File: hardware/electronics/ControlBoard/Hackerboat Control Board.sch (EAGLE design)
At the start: 178 parts, among them J3 3-1437664-0, U1 IPS6044, U14 TPS54331, U15 TPS54331, U2 ARDUINO-MEGAFULL, U3 IPS6044, U4 IPS6044, U5 IPS6044

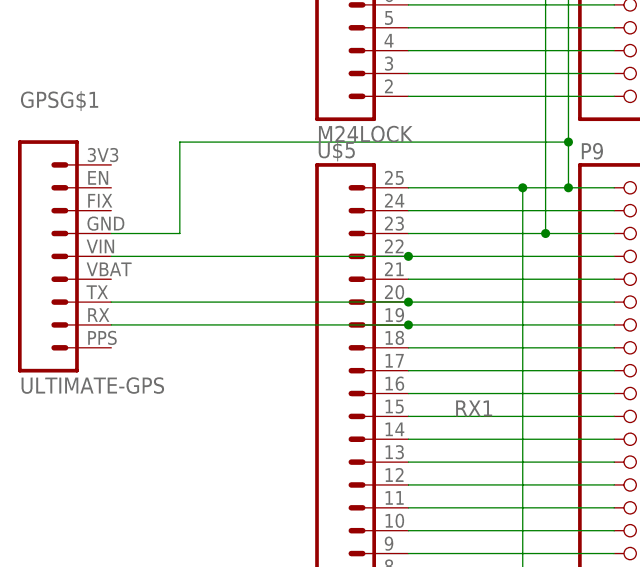
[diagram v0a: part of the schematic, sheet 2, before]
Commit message: Added hardware test code Various modifications to 'as-built' condition Added TODO.md
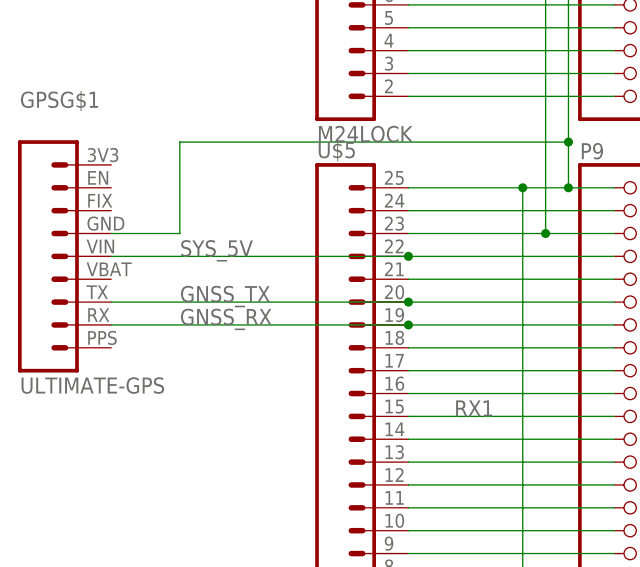
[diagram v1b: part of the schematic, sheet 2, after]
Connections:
- net N$1 renamed GNSS_RX
- net N$2 renamed GNSS_TX
- net N$67 renamed SYS_5V
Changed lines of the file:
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@@
 </segment>
 </net>
-<net name="N$1" class="0">
+<net name="GNSS_RX" class="0">
 <segment>
 <pinref part="GPS" gate="G$1" pin="2"/>
@@
 <wire x1="63.5" y1="106.68" x2="86.36" y2="106.68" width="0.1524" layer="91"/>
 <junction x="63.5" y="106.68"/>
-</segment>
-</net>
-<net name="N$2" class="0">
+<label x="38.1" y="106.68" size="1.778" layer="95"/>
+</segment>
+</net>
+<net name="GNSS_TX" class="0">
 <segment>
 <pinref part="GPS" gate="G$1" pin="3"/>
@@
 <wire x1="63.5" y1="109.22" x2="86.36" y2="109.22" width="0.1524" layer="91"/>
 <junction x="63.5" y="109.22"/>
+<label x="38.1" y="109.22" size="1.778" layer="95"/>
 </segment>
 </net>
@@
 </segment>
 </net>
-<net name="N$67" class="0">
+<net name="SYS_5V" class="0">
 <segment>
 <pinref part="GPS" gate="G$1" pin="5"/>
@@
 <wire x1="30.48" y1="114.3" x2="63.5" y2="114.3" width="0.1524" layer="91"/>
 <junction x="63.5" y="114.3"/>
-</segment>
-</net>
+<label x="38.1" y="114.3" size="1.778" layer="95"/>
+</segment>
+</net>

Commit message: Initial trimming of unnecessary parts in preparation for serious work. Keeping the power supply circuits, BBB connection, IMU, and GPS.
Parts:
- removed AUX, RELAY: 1751303, con-phoenix-350:1751303
- removed C1, C10, C11, C12, C2, C3, C4, C9: 1n, resistor:C-EUC0603
- removed C13, C14, C15, C16, C5, C6, C7, C8: 100n, resistor:C-EUC0603
- removed D1, D2: 3.3V, SparkFun-DiscreteSemi:DIODE-ZENER3.3V
- removed D10, D11, D12, D13, D14, D15, D16, D17, D18, D19, D20, D21, D22, D23, D24, D25, D26, D27, D28, D29, D3, D30, D31, D32, D33, D34, D4, D5, D6, D7, D8, D9: (no value), adafruit:DIODESOD-123
- removed F1, F4, F5, F6, F7, F8, F9: (no value), adafruit:PTCFUSE-1206
- removed H5, H6: MOUNT-PAD-ROUND5.5, holes:MOUNT-PAD-ROUND5.5
- removed HTU21D: HTU21D, sparkfun-sensor-boards:HTU21D
- removed I1/V2, I2/V3, I3/V4, I4: (no value), SparkFun-Connectors:M04LOCK_LONGPADS
- removed JP10, JP11, JP12, JP13, JP14: (no value), SparkFun-Connectors:M08LOCK
- removed JP15, JP16: M16LOCK, SparkFun-Connectors:M16LOCK
- removed JP17: (no value), SparkFun-Connectors:M06LOCK
- removed LED10, LED3, LED4, LED5, LED6, LED7, LED8, LED9: (no value), adafruit:LEDCHIPLED_0805
- removed R1, R2: 1K, resistor:R-EU_R0603
- removed R10, R17, R18, R9: 100K, res-cap-arrays:4R-NCTS742C083
- removed R11, R12, R13, R14, R15, R16, R3, R5, R6, R7, R8: 10K, res-cap-arrays:4R-NCTS742C083
- removed R25, R31, R32, R33, R34, R35, R36, R37: (no value), resistor:R-EU_R0603
- removed R29: 15K, resistor:R-EU_R0603
- removed R30: 10K, resistor:R-EU_R0603
- removed R4: 10k, res-cap-arrays:4R-NCTS742C083
- removed SERVO_AUX1, SERVO_AUX2, STEERING: (no value), SparkFun-Connectors:M03LOCK_LONGPADS
- removed U1, U3, U4, U5: IPS6044, logos-faves:IPS6044
- removed U10, U11, U12, U13, U6, U7, U8, U9: (no value), allegro3:ACS712
- removed U2: ARDUINO-MEGAFULL, SparkFun-Boards:ARDUINO-MEGAFULL
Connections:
- removed net +5V/1: C24.1, C25.1, L1.2, R22.2, R38.2, U$1.VDD_5V@1, U$1.VDD_5V@2, U$2.23, U$5.23
- removed net 13: JP14.3, U2.13
- removed net AUX1: JP15.9, R11A.1, U2.36
- removed net AUX1FB: JP16.9, R11B.1, U2.37
- removed net AUX1I: JP12.7, U2.A9, U6.VIO
- removed net AUX2: JP16.10, R12B.1, U2.35
- removed net AUX2FB: JP15.10, R11D.1, U2.34
- removed net AUX2I: JP12.8, U2.A8, U7.VIO
- removed net AUX3: JP15.11, R12C.1, U2.32
- removed net AUX3FB: JP16.11, R12D.1, U2.33
- removed net AUX3I: JP11.1, U2.A7, U8.VIO
- removed net AUX4: JP16.12, R13D.1, U2.31
- removed net AUX4FB: JP15.12, R13C.1, U2.30
- removed net AUX4I: JP11.2, U2.A6, U9.VIO
- removed net AUX5: JP15.13, R14A.1, U2.28
- removed net AUX5FB: JP16.13, R14B.1, U2.29
- removed net AUX5I: JP11.3, U10.VIO, U2.A5
- removed net AUX6: JP16.14, R15B.1, U2.27
- removed net AUX6FB: JP15.14, R14D.1, U2.26
- removed net AUX6I: JP11.4, U11.VIO, U2.A4
- removed net AUX7: JP15.15, R15C.1, U2.24
- removed net AUX7FB: JP16.15, R16A.1, U2.25
- removed net AUX7I: JP11.5, U12.VIO, U2.A3
- removed net AUX8: JP16.16, R16D.1, U2.23
- removed net AUX8FB: JP15.16, R16C.1, U2.22
- removed net AUX8I: JP11.6, U13.VIO, U2.A2
- removed net I1: I1/V2.2, JP12.6, U2.A10
- removed net I2: I2/V3.2, JP12.3, U2.A13
- removed net I3: I3/V4.2, JP12.4, U2.A12
- removed net I4: I4.2, JP12.5, U2.A11
- removed net N$10: D7.C, D8.A, LED5.A, R9B.1, RELAY-3.K, U1.OUT3@0, U1.OUT3@1, U1.OUT3@2
- removed net N$100: JP14.7, U2.9
- removed net N$101: JP14.6, U2.10
- removed net N$102: JP14.5, U2.11
- removed net N$103: JP14.4, U2.12
- removed net N$11: D10.A, D9.C, LED6.A, R9A.1, RELAY-4.K, U1.OUT4@0, U1.OUT4@1, U1.OUT4@2
- removed net N$12: R4A.2, U1.IN1
- removed net N$13: R5B.2, U1.IN2
- removed net N$14: R5C.2, U1.IN3
- removed net N$15: R3D.2, U1.IN4
- removed net N$16: R4B.2, R4C.2, U1.DG1
- removed net N$17: R4D.2, R5A.2, U1.DG2
- removed net N$178: LED3.C, R25.2
- removed net N$179: LED4.C, R31.2
- removed net N$18: R3A.2, R5D.2, U1.DG3
- removed net N$180: LED5.C, R32.2
- removed net N$181: LED6.C, R33.2
- removed net N$186: LED7.C, R34.2
- removed net N$187: LED8.C, R35.2
- removed net N$188: LED9.C, R36.2
- removed net N$189: LED10.C, R37.2
- removed net N$19: R3B.2, R3C.2, U1.DG4
- removed net N$20: R7B.2, U3.IN2
- removed net N$21: R6D.2, R7A.2, U3.DG2
- removed net N$22: R6B.2, R6C.2, U3.DG1
- removed net N$23: R7D.2, R8A.2, U3.DG3
- removed net N$24: R8B.2, R8C.2, U3.DG4
- removed net N$25: D11.C, D12.A, LED7.A, R10D.1, RELAY-5.K, U3.OUT1@0, U3.OUT1@1, U3.OUT1@2
- removed net N$26: D13.C, D14.A, LED8.A, R10C.1, RELAY-6.K, U3.OUT2@0, U3.OUT2@1, U3.OUT2@2
- removed net N$27: D15.C, D16.A, LED9.A, R10B.1, RELAY-7.K, U3.OUT3@0, U3.OUT3@1, U3.OUT3@2
- removed net N$28: D17.C, D18.A, LED10.A, R10A.1, RELAY-8.K, U3.OUT4@0, U3.OUT4@1, U3.OUT4@2
- removed net N$29: D25.C, D26.A, R17A.1, U4.OUT4@0, U4.OUT4@1, U4.OUT4@2, U9.IP+@0, U9.IP+@1
- removed net N$3: JP13.4, R1.1, U2.18(TX1)
- removed net N$30: AUX-2.K, U7.IP-@0, U7.IP-@1
- removed net N$31: AUX-3.K, U8.IP-@0, U8.IP-@1
- removed net N$32: AUX-4.K, U9.IP-@0, U9.IP-@1
- removed net N$33: AUX-5.K, U10.IP-@0, U10.IP-@1
- removed net N$34: D19.C, D20.A, R17D.1, U4.OUT1@0, U4.OUT1@1, U4.OUT1@2, U6.IP+@0, U6.IP+@1
- removed net N$35: D21.C, D22.A, R17C.1, U4.OUT2@0, U4.OUT2@1, U4.OUT2@2, U7.IP+@0, U7.IP+@1
- removed net N$36: D23.C, D24.A, R17B.1, U4.OUT3@0, U4.OUT3@1, U4.OUT3@2, U8.IP+@0, U8.IP+@1
- removed net N$37: AUX-1.K, U6.IP-@0, U6.IP-@1
- removed net N$38: R11A.2, U4.IN1
- removed net N$39: R12B.2, U4.IN2
- removed net N$4: JP10.7, R2.2, U2.1(TX0)
- removed net N$40: R12C.2, U4.IN3
- removed net N$41: R13D.2, U4.IN4
- removed net N$42: R11B.2, R11C.2, U4.DG1
- removed net N$43: R11D.2, R12A.2, U4.DG2
- removed net N$44: R12D.2, R13A.2, U4.DG3
- removed net N$45: R13B.2, R13C.2, U4.DG4
- removed net N$46: R14A.2, U5.IN1
- removed net N$47: R16D.2, U5.IN4
- removed net N$48: R15C.2, U5.IN3
- removed net N$49: R15B.2, U5.IN2
- removed net N$5: R6A.2, U3.IN1
- removed net N$50: R14B.2, R14C.2, U5.DG1
- removed net N$51: R14D.2, R15A.2, U5.DG2
- removed net N$52: R15D.2, R16A.2, U5.DG3
- removed net N$53: R16B.2, R16C.2, U5.DG4
- removed net N$54: D27.C, D28.A, R18D.1, U10.IP+@0, U10.IP+@1, U5.OUT1@0, U5.OUT1@1, U5.OUT1@2
- removed net N$55: D29.C, D30.A, R18C.1, U11.IP+@0, U11.IP+@1, U5.OUT2@0, U5.OUT2@1, U5.OUT2@2
- removed net N$56: D31.C, D32.A, R18B.1, U12.IP+@0, U12.IP+@1, U5.OUT3@0, U5.OUT3@1, U5.OUT3@2
- removed net N$57: D33.C, D34.A, R18A.1, U13.IP+@0, U13.IP+@1, U5.OUT4@0, U5.OUT4@1, U5.OUT4@2
- removed net N$58: AUX-6.K, U11.IP-@0, U11.IP-@1
- removed net N$59: AUX-7.K, U12.IP-@0, U12.IP-@1
- removed net N$6: R8D.2, U3.IN4
- removed net N$60: AUX-8.K, U13.IP-@0, U13.IP-@1
- removed net N$61: C1.2, U6.FILT
- removed net N$64: C2.2, U7.FILT
- removed net N$65: C3.2, U8.FILT
- removed net N$66: C4.2, U9.FILT
- removed net N$7: R7C.2, U3.IN3
- removed net N$74: C9.2, U10.FILT
- removed net N$75: C10.2, U11.FILT
- removed net N$76: C11.2, U12.FILT
- removed net N$77: C12.2, U13.FILT
- removed net N$8: D3.C, D4.A, LED3.A, R9D.1, RELAY-1.K, U1.OUT1@0, U1.OUT1@1, U1.OUT1@2
- removed net N$83: F1.2, I1/V2.1
- removed net N$86: F4.2, I2/V3.1
- removed net N$87: F5.2, I3/V4.1
- removed net N$88: F6.2, I4.1
- removed net N$89: F7.2, SERVO_AUX1.2
- removed net N$9: D5.C, D6.A, LED4.A, R9C.1, RELAY-2.K, U1.OUT2@0, U1.OUT2@1, U1.OUT2@2
- removed net N$90: F8.2, SERVO_AUX2.2
- removed net N$91: JP10.1, U2.7
- removed net N$92: JP10.2, U2.6
- removed net N$93: F9.2, STEERING.2
- removed net N$94: JP11.8, R29.1, R30.2, U2.A0
- removed net N$95: JP13.5, U2.17(RX2)
- removed net N$96: JP13.6, U2.16(TX2)
- removed net N$97: JP13.7, U2.15(RX3)
- removed net N$98: JP13.8, U2.14(TX3)
- removed net N$99: JP14.8, U2.8
- removed net RELAY1: JP15.1, R4A.1, U2.52
- removed net RELAY1FB: JP16.1, R4B.1, U2.53
- removed net RELAY2: JP16.2, R5B.1, U2.51
- removed net RELAY2FB: JP15.2, R5A.1, U2.50
- removed net RELAY3: JP15.3, R5C.1, U2.48
- removed net RELAY3FB: JP16.3, R5D.1, U2.49
- removed net RELAY4: JP16.4, R3D.1, U2.47
- removed net RELAY4FB: JP15.4, R3C.1, U2.46
- removed net RELAY5: JP15.5, R6A.1, U2.44
- removed net RELAY5FB: JP16.5, R6B.1, U2.45
- removed net RELAY6: JP16.6, R7B.1, U2.43
- removed net RELAY6FB: JP15.6, R6D.1, U2.42
- removed net RELAY7: JP15.7, R7C.1, U2.40
- removed net RELAY7FB: JP16.7, R7D.1, U2.41
- removed net RELAY8: JP16.8, R8D.1, U2.39
- removed net RELAY8FB: JP15.8, R8C.1, U2.38
- removed net SCL: HTU21D.4, IMUG$1.4, JP13.1, R19.1, U2.21(SCL)
- removed net SDA: HTU21D.3, IMUG$1.5, JP13.2, R20.1, U2.20(SDA)
- removed net SERVO_AUX1: JP10.4, SERVO_AUX1.3, U2.4
- removed net SERVO_AUX2: JP10.3, SERVO_AUX2.3, U2.5
- removed net STEERING: JP10.5, STEERING.3, U2.3
- removed net V2: I1/V2.3, JP11.7, U2.A1
- removed net V3: I2/V3.3, JP12.1, U2.A15
- removed net V4: I3/V4.3, JP12.2, U2.A14
- new net N$196: IMUG$1.5, R20.1
- new net N$197: IMUG$1.4, R19.1
- net +12V: no longer D10.C, D12.C, D14.C, D16.C, D18.C, D20.C, D22.C, D24.C, D26.C, D28.C, D30.C, D32.C, D34.C, D4.C, D6.C, D8.C, JP17.6, R10A.2, R10B.2, R10C.2, R10D.2, R17A.2, R17B.2, R17C.2, R17D.2, R18A.2, R18B.2, R18C.2, R18D.2, R29.2, R9A.2, R9B.2, R9C.2, R9D.2, U1.VCC@0, U1.VCC@1, U1.VCC@2, U1.VCC@3, U2.VIN, U3.VCC@0, U3.VCC@1, U3.VCC@2, U3.VCC@3, U4.VCC@0, U4.VCC@1, U4.VCC@2, U4.VCC@3, U5.VCC@0, U5.VCC@1, U5.VCC@2, U5.VCC@3
- net +3V3: no longer HTU21D.1, JP17.2, U2.3.3V
- net +5V: now also C24.1, C25.1, L1.2, R22.2, R38.2, U$1.VDD_5V@1, U$1.VDD_5V@2, U$2.23, U$5.23; no longer C13.2, C14.2, C15.2, C16.2, C5.2, C6.2, C7.2, C8.2, F1.1, F4.1, F5.1, F6.1, JP17.3, R11C.1, R12A.1, R13A.1, R13B.1, R14C.1, R15A.1, R15D.1, R16B.1, R3A.1, R3B.1, R4C.1, R4D.1, R6C.1, R7A.1, R8A.1, R8B.1, U10.VCC, U11.VCC, U12.VCC, U13.VCC, U2.5V@0, U2.5V@1, U2.5V@2, U6.VCC, U7.VCC, U8.VCC, U9.VCC
- net 7V4: no longer F7.1, F8.1, F9.1
- net GND: no longer C1.1, C10.1, C11.1, C12.1, C13.1, C14.1, C15.1, C16.1, C2.1, C3.1, C4.1, C5.1, C6.1, C7.1, C8.1, C9.1, D1.A, D11.A, D13.A, D15.A, D17.A, D19.A, D2.A, D21.A, D23.A, D25.A, D27.A, D29.A, D3.A, D31.A, D33.A, D5.A, D7.A, D9.A, H5.MOUNT, H6.MOUNT, HTU21D.2, I1/V2.4, I2/V3.4, I3/V4.4, I4.4, JP17.4, JP17.5, R25.1, R30.1, R31.1, R32.1, R33.1, R34.1, R35.1, R36.1, R37.1, SERVO_AUX1.1, SERVO_AUX2.1, STEERING.1, U1.GND@1, U1.GND@2, U1.GND@3, U1.GND@4, U10.GND, U11.GND, U12.GND, U13.GND, U2.GND@0, U2.GND@1, U2.GND@2, U2.GND@3, U2.GND@4, U3.GND@1, U3.GND@2, U3.GND@3, U3.GND@4, U4.GND@1, U4.GND@2, U4.GND@3, U4.GND@4, U5.GND@1, U5.GND@2, U5.GND@3, U5.GND@4, U6.GND, U7.GND, U8.GND, U9.GND
- net RX0: no longer JP10.8, U2.0(RX0)
- net RX1: no longer JP13.3, U2.19(RX1)
- net SERVO_EN: no longer JP10.6, U2.2
- net TX0: no longer D2.C, R2.1
- net TX1: no longer D1.C, R1.2

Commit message: First cut at the system block diagram
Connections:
- removed net N$118: U$1.VDD_3V3EXP@2, U$2.24
- removed net N$71: U$1.VDD_3V3EXP@1, U$5.24
- net +3V3: now also U$1.VDD_3V3EXP@1, U$1.VDD_3V3EXP@2, U$2.24, U$5.24
- net GND: no longer GPSG$1.6
- net GNSS_RX: no longer GPSG$1.2
- net GNSS_TX: no longer GPSG$1.3
- net SYS_5V: no longer GPSG$1.5
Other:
- note added: "Grounding"
- note added: "Main Systems Power"
- note added: "Servo Power"

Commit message: Everything in except the 15V boost converter and a couple of connectors
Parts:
- removed 5V/1-STAT: (no value), adafruit:LEDCHIPLED_0805
- added 5V-STAT: (no value), adafruit:LEDCHIPLED_0805
- added ACC_POWER: (no value), pinhead-1:PINHD-2X8_2.54
- added BBB_CONSOLE: FTDI_BASICPTH, SparkFun-Connectors:FTDI_BASICPTH
- added C1, C2, C3, C4, C5, C6: (no value), resistor:C-EUC0603
- added C10, C11, C12, C13, C14, C15, C16, C35, C36, C37, C38, C39, C7, C8, C9: 100n, resistor:C-EUC0603
- added D1, D10, D11, D12, D13, D14, D15, D16, D17, D18, D19, D2, D3, D4, D5, D6, D7, D8, D9: (no value), adafruit:DIODESOD-123
- added IC1: 74AHC1G08DBV, 74xx-little-us:74AHC1G08DBV
- added J1, J2: (no value), SparkFun-Connectors:M03LOCK
- added J4: (no value), SparkFun-Connectors:M05LOCK
- added J5: (no value), SparkFun-Connectors:M09LOCK
- added J6: (no value), SparkFun-Connectors:M10LOCK
- added J7: (no value), SparkFun-Connectors:M18_
- added MOTOR-CTRL-RELAYS: (no value), SparkFun-Connectors:DB9FEMALE
- added POE-DEVICE, POE-LAN: RJ45, SparkFun-Connectors:RJ45-8PTH
- added POWER_INPUT: 3-1437664-0, logos-headers:3-1437664-0
- added POWER_MONITOR: (no value), pinhead-1:PINHD-2X6_2.54
- added POWER_STATE: HEADER_POS5_70555, con-molex-c-grid-sl:HEADER_POS5_70555
- added R1, R13, R14, R15, R2, R25, R29, R3, R30, R34, R35, R36, R42, R43, R44, R48, R69, R7, R70, R71, R75, R76, R77, R8, R81, R82, R83, R9: 10K, resistor:R-EU_R0603
- added R10, R16, R31, R37, R4, R45, R72, R78, R84: 100K, resistor:R-EU_R0603
- added R11, R17, R32, R40, R46, R5, R55, R73, R79, R85: 0R05, resistor:R-EU_R2512
- added R12, R18, R33, R41, R47, R56, R6, R74, R80, R86: 33K, resistor:R-EU_R0603
- added R49, R50: (no value), resistor:R-EU_R0603
- added R51, R52, R53, R54: 4u7, resistor:R-EU_R0603
- added S1: FONA, adafruit-sensor-boards:FONA
- added SERIAL_CONSOLE: HEADER_POS4_70555, con-molex-c-grid-sl:HEADER_POS4_70555
- added STATUS_LIGHTS, STEERING: HEADER_POS3_70555, con-molex-c-grid-sl:HEADER_POS3_70555
- added U1, U11, U2, U20, U22, U24, U4, U6, U8: IPS6041G, hackerbot:IPS6041G
- added U10, U12, U21, U23, U25, U27, U3, U5, U7, U9: INA169, logos-power:INA169
- added U13, U16, U17: (no value), adafruit:TXB0108PWR
- added U18, U19: ADC128D818, ti-stuff:ADC128D818
- added U26: (no value), adafruit:TXS0102
- J3: value 3-1437664-0 -> (none); device logos-headers:3-1437664-0 -> SparkFun-Connectors:M04LOCK
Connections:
- net N$109 renamed BBB_MISO
- net N$168 renamed BBB_SCLK
- net N$169 renamed BBB_MOSI
- net RX1 renamed N$21
- net TX1 renamed BBB_STAT_LIGHT_3V3
- removed net 7V4: C26.1, C27.1, L2.2, R27.2, R39.2
- removed net N$105: U$1.AIN1, U$2.6
- removed net N$111: U$1.I2C2_SDA, U$2.16
- removed net N$112: U$1.I2C1_SDA, U$2.17
- removed net N$113: U$1.EHRPWM1B, U$2.18
- removed net N$114: U$1.EHRPWM1A, U$2.19
- removed net N$115: U$1.GPIO1_28, U$2.20
- removed net N$116: U$1.SYS_RESETN, U$2.21
- removed net N$122: U$1.GPIO2_13, U$3.5
- removed net N$123: U$1.UART5_RXD, U$3.6
- removed net N$124: U$1.UART3_CTSN, U$3.7
- removed net N$125: U$1.UART3_RTSN, U$3.8
- removed net N$126: U$1.UART5_RTSN, U$3.9
- removed net N$127: U$1.GPIO2_25, U$3.10
- removed net N$128: U$1.GPIO2_24, U$3.11
- removed net N$129: U$1.GPIO1_29, U$3.12
- removed net N$130: U$1.GPIO1_1, U$3.13
- removed net N$131: U$1.GPIO1_5, U$3.14
- removed net N$132: U$1.GPIO1_31, U$3.15
- removed net N$133: U$1.GPIO2_1, U$3.16
- removed net N$134: U$1.GPIO1_14, U$3.17
- removed net N$135: U$1.GPIO0_26, U$3.18
- removed net N$136: U$1.GPIO1_12, U$3.19
- removed net N$137: U$1.TIMER6, U$3.20
- removed net N$138: U$1.TIMER7, U$3.21
- removed net N$139: U$1.GPIO1_3, U$3.22
- removed net N$140: U$1.GPIO1_7, U$3.23
- removed net N$145: U$1.UART5_TXD, U$4.6
- removed net N$147: U$1.UART4_RTSN, U$4.8
- removed net N$148: U$1.UART5_CTSN, U$4.9
- removed net N$149: U$1.GPIO2_23, U$4.10
- removed net N$150: U$1.GPIO2_22, U$4.11
- removed net N$151: U$1.GPIO1_0, U$4.12
- removed net N$152: U$1.GPIO1_4, U$4.13
- removed net N$153: U$1.GPIO1_30, U$4.14
- removed net N$154: U$1.EHRPWM2A, U$4.15
- removed net N$155: U$1.GPIO0_27, U$4.16
- removed net N$156: U$1.GPIO1_15, U$4.17
- removed net N$157: U$1.EHRPWM2B, U$4.18
- removed net N$158: U$1.GPIO1_13, U$4.19
- removed net N$159: U$1.TIMER5, U$4.20
- removed net N$160: U$1.TIMER4, U$4.21
- removed net N$161: U$1.GPIO1_2, U$4.22
- removed net N$162: U$1.GPIO1_6, U$4.23
- removed net N$173: U$1.I2C2_SCL, U$5.16
- removed net N$174: U$1.I2C1_SCL, U$5.17
- removed net N$175: U$1.GPIO1_16, U$5.18
- removed net N$196: IMUG$1.5, R20.1
- removed net N$197: IMUG$1.4, R19.1
- removed net RX0: U$1.UART1_TXD, U$2.14
- removed net SERVO_EN: U15.EN
- removed net TX0: U$1.UART1_RXD, U$2.13
- new net +15V: ACC_POWER.13, ACC_POWER.14, POE-DEVICE.4, POE-DEVICE.5
- new net +7V4: ACC_POWER.15, ACC_POWER.16, J1.1, R55.2, STEERING.1, U27.VIN-
- new net +7V4_OUT: C26.1, C27.1, L2.2, R27.2, R39.2, R55.1, U27.VIN+
- new net AUX_ADC_0: POWER_MONITOR.10, U19.IN5
- new net AUX_ADC_1: POWER_MONITOR.11, U19.IN6
- new net AUX_GPIO_0_3V3: U$1.GPIO1_30, U$4.14, U16.A8
- new net AUX_GPIO_0_5V: U16.B8
- new net AUX_GPIO_1_3V3: U$1.GPIO1_4, U$4.13, U17.A3
- new net AUX_GPIO_1_5V: U17.B3
- new net AUX_GPIO_2_3V3: U$1.GPIO1_0, U$4.12, U17.A4
- new net AUX_GPIO_2_5V: U17.B4
- new net AUX_GPIO_3_3V3: U$1.GPIO2_22, U$4.11, U17.A5
- new net AUX_GPIO_3_5V: U17.B5
- new net AUX_GPIO_4_3V3: U$1.GPIO2_23, U$4.10, U17.A6
- new net AUX_GPIO_4_5V: U17.B6
- new net AUX_GPIO_5_3V3: U$1.UART4_RTSN, U$4.8, U17.A7
- new net AUX_GPIO_5_5V: U17.B7
- new net BATMON: D13.C, R49.1, R50.2, U$1.AIN1, U$2.6
- new net BBB_I2C_1_SCL: IMUG$1.4, J6.4, R19.1, U$1.I2C1_SCL, U$5.17
- new net BBB_I2C_1_SDA: IMUG$1.5, J6.5, R20.1, U$1.I2C1_SDA, U$2.17
- new net BBB_I2C_2_SCL: R53.1, U$1.I2C2_SCL, U$5.16, U26.A2
- new net BBB_I2C_2_SDA: R54.1, U$1.I2C2_SDA, U$2.16, U26.A1
- new net BBB_RESET_3V3: R48.2, U$1.SYS_RESETN, U$2.21, U16.A7
- new net BBB_RESET_5V: U16.B7
- new net BBB_STATUS_LIGHTS_5V: J2.2, STATUS_LIGHTS.2
- new net BBB_STATUS_LIGHT_3V3: U16.A6
- new net BBB_STATUS_LIGHT_5V: U16.B6
- new net BBB_UART0_DTR: BBB_CONSOLE.1, J3.1, SERIAL_CONSOLE.1
- new net BBB_UART0_RX: BBB_CONSOLE.2, J3.2, SERIAL_CONSOLE.2
- new net BBB_UART0_TX: BBB_CONSOLE.3, J3.3, SERIAL_CONSOLE.3
- new net BBB_UART1_RX_3V3: U$1.UART1_TXD, U$2.14, U17.A1
- new net BBB_UART1_RX_5V: U17.B1
- new net BBB_UART1_TX_3V3: U$1.UART1_RXD, U$2.13, U17.A2
- new net BBB_UART1_TX_5V: U17.B2
- new net CELL_CTS: J7.9, S1G$1.9, U$1.UART5_CTSN, U$4.9
- new net CELL_KEY: J7.8, S1G$1.8, U$1.GPIO2_13, U$3.5
- new net CELL_NET_STATUS: J7.5, S1G$1.5, U$1.UART3_RTSN, U$3.8
- new net CELL_POWER_STATUS: J7.6, S1G$1.6, U$1.GPIO2_24, U$3.11
- new net CELL_RESET: J7.14, S1G$1.14, U$1.UART3_CTSN, U$3.7
- new net CELL_RING: J7.7, S1G$1.7, U$1.GPIO2_25, U$3.10
- new net CELL_RTS: J7.11, S1G$1.11, U$1.UART5_RTSN, U$3.9
- new net CELL_RX: J7.13, S1G$1.13, U$1.UART5_TXD, U$4.6
- new net CELL_TX: J7.12, S1G$1.12, U$1.UART5_RXD, U$3.6
- new net CHARGE_CURRENT: POWER_MONITOR.7, U19.IN4
- new net CHARGE_VOLTAGE: POWER_MONITOR.6, U19.IN3
- new net DISARM_RELAY_IN_3V3: U$1.GPIO1_5, U$3.14, U16.A5
- new net DISARM_RELAY_IN_5V: J4.2, POWER_STATE.2, U16.B5
- new net ENABLE_RELAY_IN_3V3: U$1.GPIO1_31, U$3.15, U16.A4
- new net ENABLE_RELAY_IN_5V: IC1A.I1, J4.1, POWER_STATE.1, U16.B4
- new net GNSS_ENABLE: GPSG$1.8, J5.8, U$1.GPIO1_28, U$2.20
- new net GNSS_FIX: GPSG$1.7, J5.6, U$1.GPIO1_16, U$5.18
- new net MOT_CURRENT: POWER_MONITOR.3, U19.IN1
- new net MOT_VOLTAGE: POWER_MONITOR.2, U19.IN2
- new net N$1: R1.2, R2.1, U1.DGS
- new net N$10: R25.2, R29.1, U6.DGS
- new net N$11: R30.2, U6.IN
- new net N$12: R31.1, R32.1, U6.OUT, U7.VIN+
- new net N$13: R34.2, R35.1, U8.DGS
- new net N$14: R36.2, U8.IN
- new net N$15: R37.1, R40.1, U10.VIN+, U8.OUT
- new net N$16: R42.2, R43.1, U11.DGS
- new net N$17: R44.2, U11.IN
- new net N$18: R45.1, R46.1, U11.OUT, U12.VIN+
- new net N$19: GPSG$1.1, J5.1
- new net N$2: R3.2, U1.IN
- new net N$20: GPSG$1.4, J5.7
- new net N$23: R52.1, U18.SDA, U19.SDA, U26.B1
- new net N$24: R69.2, R70.1, U20.DGS
- new net N$25: R71.2, U20.IN
- new net N$26: R72.1, R73.1, U20.OUT, U21.VIN+
- new net N$27: R51.1, U18.SCL, U19.SCL, U26.B2
- new net N$28: IMUG$1.2, J6.2
- new net N$29: IMUG$1.6, J6.6
- new net N$3: R4.1, R5.1, U1.OUT, U9.VIN+
- new net N$30: IMUG$1.7, J6.7
- new net N$31: IMUG$1.8, J6.8
- new net N$32: IMUG$1.9, J6.9
- new net N$33: IMUG$1.10, J6.10
- new net N$34: R75.2, R76.1, U22.DGS
- new net N$35: GPSG$1.9, J5.9
- new net N$36: IC1A.O, U15.EN
- new net N$37: J7.2, S1G$1.2
- new net N$38: J7.3, S1G$1.3
- new net N$39: J7.4, S1G$1.4
- new net N$4: R7.2, R8.1, U2.DGS
- new net N$40: J7.10, S1G$1.10
- new net N$41: J7.17, S1G$1.17
- new net N$42: J7.1, S1G$1.1
- new net N$43: POE-DEVICE.1, POE-LAN.1
- new net N$44: POE-DEVICE.2, POE-LAN.2
- new net N$45: POE-DEVICE.3, POE-LAN.3
- new net N$48: R77.2, U22.IN
- new net N$49: R78.1, R79.1, U22.OUT, U23.VIN+
- new net N$5: R9.2, U2.IN
- new net N$50: R81.2, R82.1, U24.DGS
- new net N$51: R83.2, U24.IN
- new net N$52: R84.1, R85.1, U24.OUT, U25.VIN+
- new net N$54: POE-DEVICE.6, POE-LAN.6
- new net N$6: R10.1, R11.1, U2.OUT, U3.VIN+
- new net N$7: R13.2, R14.1, U4.DGS
- new net N$8: R15.2, U4.IN
- new net N$9: R16.1, R17.1, U4.OUT, U5.VIN+
- new net RELAY_CURRENT_0: R6.2, U18.IN0, U9.OUT
- new net RELAY_CURRENT_1: R12.2, U18.IN1, U3.OUT
- new net RELAY_CURRENT_2: R18.2, U18.IN2, U5.OUT
- new net RELAY_CURRENT_3: R33.2, U18.IN3, U7.OUT
- new net RELAY_CURRENT_4: R41.2, U10.OUT, U18.IN4
- new net RELAY_CURRENT_5: R47.2, U12.OUT, U18.IN5
- new net RELAY_CURRENT_DISARM: R74.2, U18.IN6, U21.OUT
- new net RELAY_CURRENT_ENABLE: R86.2, U18.IN7, U25.OUT
- new net RELAY_CURRENT_HORN: R80.2, U19.IN0, U23.OUT
- new net RELAY_DISARM_3V3: U$1.GPIO1_15, U$4.17, U13.A7
- new net RELAY_DISARM_5V: R71.1, U13.B7
- new net RELAY_DISARM_FAULT: R69.1, U$1.GPIO1_14, U$3.17
- new net RELAY_ENABLE_3V3: U$1.GPIO1_1, U$3.13, U16.A1
- new net RELAY_ENABLE_5V: R83.1, U16.B1
- new net RELAY_ENABLE_FAULT: R81.1, U$1.GPIO1_29, U$3.12
- new net RELAY_FAULT_0: R1.1, U$1.GPIO1_7, U$3.23
- new net RELAY_FAULT_1: R7.1, U$1.GPIO1_3, U$3.22
- new net RELAY_FAULT_2: R13.1, U$1.TIMER7, U$3.21
- new net RELAY_FAULT_3: R25.1, U$1.TIMER6, U$3.20
- new net RELAY_FAULT_4: R34.1, U$1.GPIO1_12, U$3.19
- new net RELAY_FAULT_5: R42.1, U$1.GPIO0_26, U$3.18
- new net RELAY_HORN_3V3: U$1.GPIO0_27, U$4.16, U13.A8
- new net RELAY_HORN_5V: R77.1, U13.B8
- new net RELAY_HORN_FAULT: R75.1, U$1.GPIO2_1, U$3.16
- new net RELAY_IN_0_3V3: U$1.GPIO1_6, U$4.23, U13.A1
- new net RELAY_IN_0_5V: R3.1, U13.B1
- new net RELAY_IN_1_3V3: U$1.GPIO1_2, U$4.22, U13.A2
- new net RELAY_IN_1_5V: R9.1, U13.B2
- new net RELAY_IN_2_3V3: U$1.TIMER4, U$4.21, U13.A3
- new net RELAY_IN_2_5V: R15.1, U13.B3
- new net RELAY_IN_3_3V3: U$1.TIMER5, U$4.20, U13.A4
- new net RELAY_IN_3_5V: R30.1, U13.B4
- new net RELAY_IN_4_3V3: U$1.GPIO1_13, U$4.19, U13.A5
- new net RELAY_IN_4_5V: R36.1, U13.B5
- new net RELAY_IN_5_3V3: U$1.EHRPWM2B, U$4.18, U13.A6
- new net RELAY_IN_5_5V: R44.1, U13.B6
- new net RELAY_OUT_0: D1.A, D2.C, MOTOR-CTRL-RELAYS.1, R5.2, U9.VIN-
- new net RELAY_OUT_1: D3.A, D4.C, MOTOR-CTRL-RELAYS.3, R11.2, U3.VIN-
- new net RELAY_OUT_2: D5.A, D6.C, MOTOR-CTRL-RELAYS.5, R17.2, U5.VIN-
- new net RELAY_OUT_3: D11.A, D12.C, MOTOR-CTRL-RELAYS.6, R32.2, U7.VIN-
- new net RELAY_OUT_4: D10.A, D9.C, MOTOR-CTRL-RELAYS.8, R40.2, U10.VIN-
- new net RELAY_OUT_5: D7.C, D8.A, MOTOR-CTRL-RELAYS.9, R46.2, U12.VIN-
- new net RELAY_OUT_DISARM: D14.A, D15.C, J4.4, POWER_STATE.4, R73.2, U21.VIN-
- new net RELAY_OUT_ENABLE: D18.A, D19.C, J4.5, POWER_STATE.5, R85.2, U25.VIN-
- new net RELAY_OUT_HORN: D16.A, D17.C, R79.2, U23.VIN-
- new net RS_485_DIR_SELECT_3V3: U$1.EHRPWM1A, U$2.19, U16.A2
- new net RS_485_DIR_SELECT_5V: U16.B2
- new net SERVO_CURRENT_MON: R56.2, U19.IN7, U27.OUT
- new net SERVO_ENABLE_3V3: U$1.EHRPWM2A, U$4.15, U16.A3
- new net SERVO_ENABLE_5V: IC1A.I0, U16.B3
- new net SERVO_RUDDER_3V3: U$1.EHRPWM1B, U$2.18, U17.A8
- new net SERVO_RUDDER_5V: J1.2, STEERING.2, U17.B8
- net +12V: now also D1.C, D10.C, D11.C, D14.C, D16.C, D18.C, D3.C, D5.C, D8.C, POWER_INPUT.2, R10.2, R16.2, R31.2, R37.2, R4.2, R45.2, R49.2, R72.2, R78.2, R84.2, U1.VCC@0, U1.VCC@1, U1.VCC@2, U1.VCC@3, U11.VCC@0, U11.VCC@1, U11.VCC@2, U11.VCC@3, U2.VCC@0, U2.VCC@1, U2.VCC@2, U2.VCC@3, U20.VCC@0, U20.VCC@1, U20.VCC@2, U20.VCC@3, U22.VCC@0, U22.VCC@1, U22.VCC@2, U22.VCC@3, U24.VCC@0, U24.VCC@1, U24.VCC@2, U24.VCC@3, U4.VCC@0, U4.VCC@1, U4.VCC@2, U4.VCC@3, U6.VCC@0, U6.VCC@1, U6.VCC@2, U6.VCC@3, U8.VCC@0, U8.VCC@1, U8.VCC@2, U8.VCC@3; no longer J3.1
- net +3V3: now also ACC_POWER.10, ACC_POWER.7, ACC_POWER.8, ACC_POWER.9, C1.1, C3.1, C5.1, C8.2, J7.15, R14.2, R2.2, R29.2, R35.2, R43.2, R48.1, R53.2, R54.2, R70.2, R76.2, R8.2, R82.2, S1G$1.15, U13.OE, U13.VCCA, U16.OE, U16.VCCA, U17.OE, U17.VCCA, U26.OE, U26.VCCA
- net +5V: now also ACC_POWER.1, ACC_POWER.2, ACC_POWER.3, ACC_POWER.4, C10.1, C11.1, C12.1, C13.2, C14.2, C15.2, C16.2, C2.1, C35.2, C36.2, C37.2, C38.2, C39.2, C4.1, C6.1, C7.1, C9.1, GPSG$1.5, IC1P.VCC, J2.1, J5.2, J6.1, J7.18, POWER_MONITOR.1, POWER_MONITOR.5, POWER_MONITOR.9, R51.2, R52.2, S1G$1.18, STATUS_LIGHTS.1, U10.VCC, U12.VCC, U13.VCCB, U16.VCCB, U17.VCCB, U18.A0, U18.VCC, U18.VREF, U19.VCC, U19.VREF, U21.VCC, U23.VCC, U25.VCC, U26.VCCB, U27.VCC, U3.VCC, U5.VCC, U7.VCC, U9.VCC
- net GND: now also 5V-STAT.C, ACC_POWER.11, ACC_POWER.12, ACC_POWER.5, ACC_POWER.6, BBB_CONSOLE.6, C1.2, C10.2, C11.2, C12.2, C13.1, C14.1, C15.1, C16.1, C2.2, C3.2, C35.1, C36.1, C37.1, C38.1, C39.1, C4.2, C5.2, C6.2, C7.2, C8.1, C9.2, D12.A, D13.A, D15.A, D17.A, D19.A, D2.A, D4.A, D6.A, D7.A, D9.A, GPSG$1.6, IC1P.GND, J1.3, J2.3, J3.4, J4.3, J5.3, J6.3, J7.16, MOTOR-CTRL-RELAYS.2, MOTOR-CTRL-RELAYS.4, MOTOR-CTRL-RELAYS.7, POE-DEVICE.7, POE-DEVICE.8, POWER_INPUT.1, POWER_MONITOR.12, POWER_MONITOR.4, POWER_MONITOR.8, POWER_STATE.3, R12.1, R18.1, R33.1, R41.1, R47.1, R50.1, R56.1, R6.1, R74.1, R80.1, R86.1, S1G$1.16, S1G$2.9, S1G$3.9, SERIAL_CONSOLE.4, STATUS_LIGHTS.3, STEERING.3, U$2.2, U$3.25, U$4.25, U$5.2, U1.GND, U10.GND, U11.GND, U12.GND, U13.GND, U16.GND, U17.GND, U18.A1, U18.GND, U19.A0, U19.A1, U19.GND, U2.GND, U20.GND, U21.GND, U22.GND, U23.GND, U24.GND, U25.GND, U26.GND, U27.GND, U3.GND, U4.GND, U5.GND, U6.GND, U7.GND, U8.GND, U9.GND; no longer 5V/1-STAT.C, J3.2
- net GNSS_RX: now also GPSG$1.2, J5.4
- net GNSS_TX: now also GPSG$1.3, J5.5
- net N$182: now also 5V-STAT.A; no longer 5V/1-STAT.A
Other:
- note added: "ANALOG TO DIGITAL CONVERTER"
- note added: "EXTERNAL CONNECTORS"
- note added: "LEVEL SHIFTERS"
- note added: "MOTOR CONTROL RELAY DRIVERS"
- note added: "STATUS RELAY DRIVERS"

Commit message: All placed and routed for the control board.
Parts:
- removed H2: MOUNT-PAD-ROUND3.2, holes:MOUNT-PAD-ROUND3.2
- added AUX_GPIO: 2X6 FEMALE, SparkFun-Connectors:M06X2PTH_FEMALE
- added BBB_RESET, RS485: HEADER_POS3_70555, con-molex-c-grid-sl:HEADER_POS3_70555
- added C40, C41, C42, C47, C48: 100n, resistor:C-EUC0603
- added C43, C44: 4u7, resistor:C-EUC1210
- added C45: 47n, resistor:C-EUC0603
- added C46: 68n, resistor:C-EUC0603
- added D20: (no value), ARD-SRG-MOT8-1a:SPARKFUN_DIODESMA
- added HORN: HEADER_POS2_70555, con-molex-c-grid-sl:HEADER_POS2_70555
- added IC2: TINY861L-20SU, atmel:TINY861L-20SU
- added IC3: 74AHC1G04DBV, 74xx-little-us:74AHC1G04DBV
- added J10, J11: (no value), SparkFun-Connectors:M03LOCK
- added J8: AVR_SPI_PRG_6PTH, SparkFun-Connectors:AVR_SPI_PRG_6PTH
- added J9: (no value), SparkFun-Connectors:M02LOCK
- added L3: 22u, logos-inductors:SRN8040
- added R57: 10K, resistor:R-EU_R0603
- added R58: 174K, resistor:R-EU_R0603
- added R59: 1K62, resistor:R-EU_R0603
- added R60: 182K, resistor:R-EU_R0603
- added R61: 16K2, resistor:R-EU_R0603
- added RC-IN-0, RC-IN-1, RC-IN-2, RC-IN-3, RC-IN-4, RC-IN-5, RC-IN-6, RC-IN-7: (no value), pinhead-1:PINHD-1X3_2.54
- added U$6: RS485SOIC, SparkFun-DigitalIC:RS485SOIC
- added U28: (no value), adafruit:TXB0108PWR
- added U29: TPS61175, logos-power:TPS61175
- C1, C2, C3, C4, C5, C6: value (none) -> 100n
- C17, C18, C28, C29: value 4u7 -> 10u
- C20, C31: value 2n -> 8n2
- C22: value (none) -> 2n4
- C23: value (none) -> 56p
- C24, C25: value (none) -> 22u
- C26, C27: value (none) -> 4u7
- C33: value (none) -> 7u5
- C34: value (none) -> 220p
- D13: value (none) -> 1V8
- L1: value NR6045 -> 10u
- L2: value NR6045 -> 22u
- R21: value (none) -> 26K7
- R22, R27: value (none) -> 10K2
- R23: value (none) -> 1K96
- R24, R38, R39: value (none) -> 1K
- R26: value (none) -> 11K5
- R28: value (none) -> 1K24
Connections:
- removed net BBB_STATUS_LIGHT_5V: U16.B6
- removed net N$144: U$1.GPIO2_12, U$4.5
- removed net N$146: U$1.UART4_CTSN, U$4.7
- new net I2C_SCL_5V: AUX_GPIO.4, R51.1, U18.SCL, U19.SCL, U26.B2
- new net I2C_SDA_5V: AUX_GPIO.3, R52.1, U18.SDA, U19.SDA, U26.B1
- new net N$46: IC2.(ADC6/AIN1)PA7, U28.A8
- new net N$47: IC2.(ADC5/AIN0)PA6, U28.A7
- new net N$53: IC2.(ADC4/AIN2)PA5, U28.A6
- new net N$55: IC2.(ADC3/ICP0)PA4, U28.A5
- new net N$56: IC2.(AREF)PA3, U28.A4
- new net N$57: IC2.(ADC2/INT1/USCK/SCL)PA2, U28.A3
- new net N$58: IC2.(ADC1/DO)PA1, U28.A2
- new net N$59: IC2.(ADC0/DI/SDA)PA0, U28.A1
- new net N$60: RC-IN-7.1, U28.B8
- new net N$61: RC-IN-6.1, U28.B7
- new net N$64: RC-IN-5.1, U28.B6
- new net N$65: RC-IN-4.1, U28.B5
- new net N$66: RC-IN-3.1, U28.B4
- new net N$67: RC-IN-2.1, U28.B3
- new net N$71: RC-IN-1.1, U28.B2
- new net N$74: RC-IN-0.1, U28.B1
- new net N$75: C46.1, R59.1
- new net N$76: R59.2, U29.COMP
- new net N$77: C45.1, U29.SS
- new net N$83: R58.2, U29.FREQ
- new net N$84: D20.A, L3.2, U29.SW@0, U29.SW@1
- new net N$85: R60.1, R61.2, U29.FB
- new net N$86: J11.2, RS485.2, U$6.A
- new net RC_MODE_SELECT: IC2.(ADC9/INT0/T0)PB6, R57.1, U$1.UART4_CTSN, U$4.7
- new net RC_RESET: IC2.(ADC10/!RESET!)PB7, J8.5, U$1.GPIO2_12, U$4.5
- net +12V: now also C43.1, L3.1, U29.EN, U29.VIN
- net +15V: now also C44.1, D20.C, R60.2
- net +3V3: now also C40.1, C41.1, IC2.AVCC, IC2.VCC, J8.2, U28.OE, U28.VCCA
- net +5V: now also AUX_GPIO.1, AUX_GPIO.2, BBB_RESET.1, C42.1, C47.1, C48.1, IC3P.VCC, J10.1, U$6.VCC, U28.VCCB
- net +7V4: now also R39.2
- net +7V4_OUT: no longer R39.2
- net AUX_GPIO_0_3V3: now also U17.A2; no longer U16.A8
- net AUX_GPIO_0_5V: now also AUX_GPIO.5, U17.B2; no longer U16.B8
- net AUX_GPIO_1_3V3: now also U17.A1; no longer U17.A3
- net AUX_GPIO_1_5V: now also AUX_GPIO.6, U17.B1; no longer U17.B3
- net AUX_GPIO_2_5V: now also AUX_GPIO.7
- net AUX_GPIO_3_3V3: now also U17.A3; no longer U17.A5
- net AUX_GPIO_3_5V: now also AUX_GPIO.8, U17.B3; no longer U17.B5
- net AUX_GPIO_4_5V: now also AUX_GPIO.9
- net AUX_GPIO_5_3V3: now also U17.A5; no longer U17.A7
- net AUX_GPIO_5_5V: now also AUX_GPIO.10, U17.B5; no longer U17.B7
- net BBB_MISO: now also IC2.(MISO/DO/OC1A)PB1, J8.1
- net BBB_MOSI: now also IC2.(MOSI/DI/SDA/!OC1A!)PB0, J8.4
- net BBB_RESET_5V: now also IC3A.O
- net BBB_SCLK: now also IC2.(SCK/SCL/!OC1B!)PB2, J8.3
- net BBB_STATUS_LIGHTS_5V: now also U16.B6
- net BBB_UART1_RX_3V3: now also U17.A7; no longer U17.A1
- net BBB_UART1_RX_5V: now also U$6.RO, U17.B7; no longer U17.B1
- net BBB_UART1_TX_3V3: now also U17.A8; no longer U17.A2
- net BBB_UART1_TX_5V: now also U$6.DI, U17.B8; no longer U17.B2
- net GND: now also AUX_GPIO.11, AUX_GPIO.12, BBB_RESET.3, C22.2, C33.2, C40.2, C41.2, C42.2, C43.2, C44.2, C45.2, C46.2, C47.2, C48.2, HORN.2, IC2.AGND, IC2.GND, IC3P.GND, J10.3, J11.3, J8.6, J9.2, R57.2, R58.1, R61.1, RC-IN-0.3, RC-IN-1.3, RC-IN-2.3, RC-IN-3.3, RC-IN-4.3, RC-IN-5.3, RC-IN-6.3, RC-IN-7.3, RS485.3, U$6.GND, U28.GND, U29.AGND, U29.NC, U29.PAD, U29.PGND@0, U29.PGND@1, U29.PGND@2, U29.SYN; no longer H2.MOUNT, R21.1, R26.1
- net N$23: now also BBB_RESET.2, IC3A.I, J10.2; no longer R52.1, U18.SDA, U19.SDA, U26.B1
- net N$27: now also J11.1, RS485.1, U$6.B; no longer R51.1, U18.SCL, U19.SCL, U26.B2
- net N$68: now also C22.1, R21.1; no longer C22.2, R21.2
- net N$70: now also R21.2; no longer C22.1
- net N$80: now also C33.1, R26.1; no longer C33.2, R26.2
- net N$81: now also R26.2; no longer C33.1
- net RELAY_OUT_HORN: now also HORN.1, J9.1
- net RS_485_DIR_SELECT_5V: now also U$6./RE, U$6.DE
- net SERVO_RUDDER_3V3: now also U16.A8; no longer U17.A8
- net SERVO_RUDDER_5V: now also U16.B8; no longer U17.B8
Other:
- note added: "+15V POWER SUPPLY"
- note added: "BEAGLEBONE"
- note added: "R/C CONTROL INPUT"
- note added: "RS485 TRANSCEIVER"
